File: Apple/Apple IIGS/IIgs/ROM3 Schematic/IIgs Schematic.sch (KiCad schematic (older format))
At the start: 0 parts

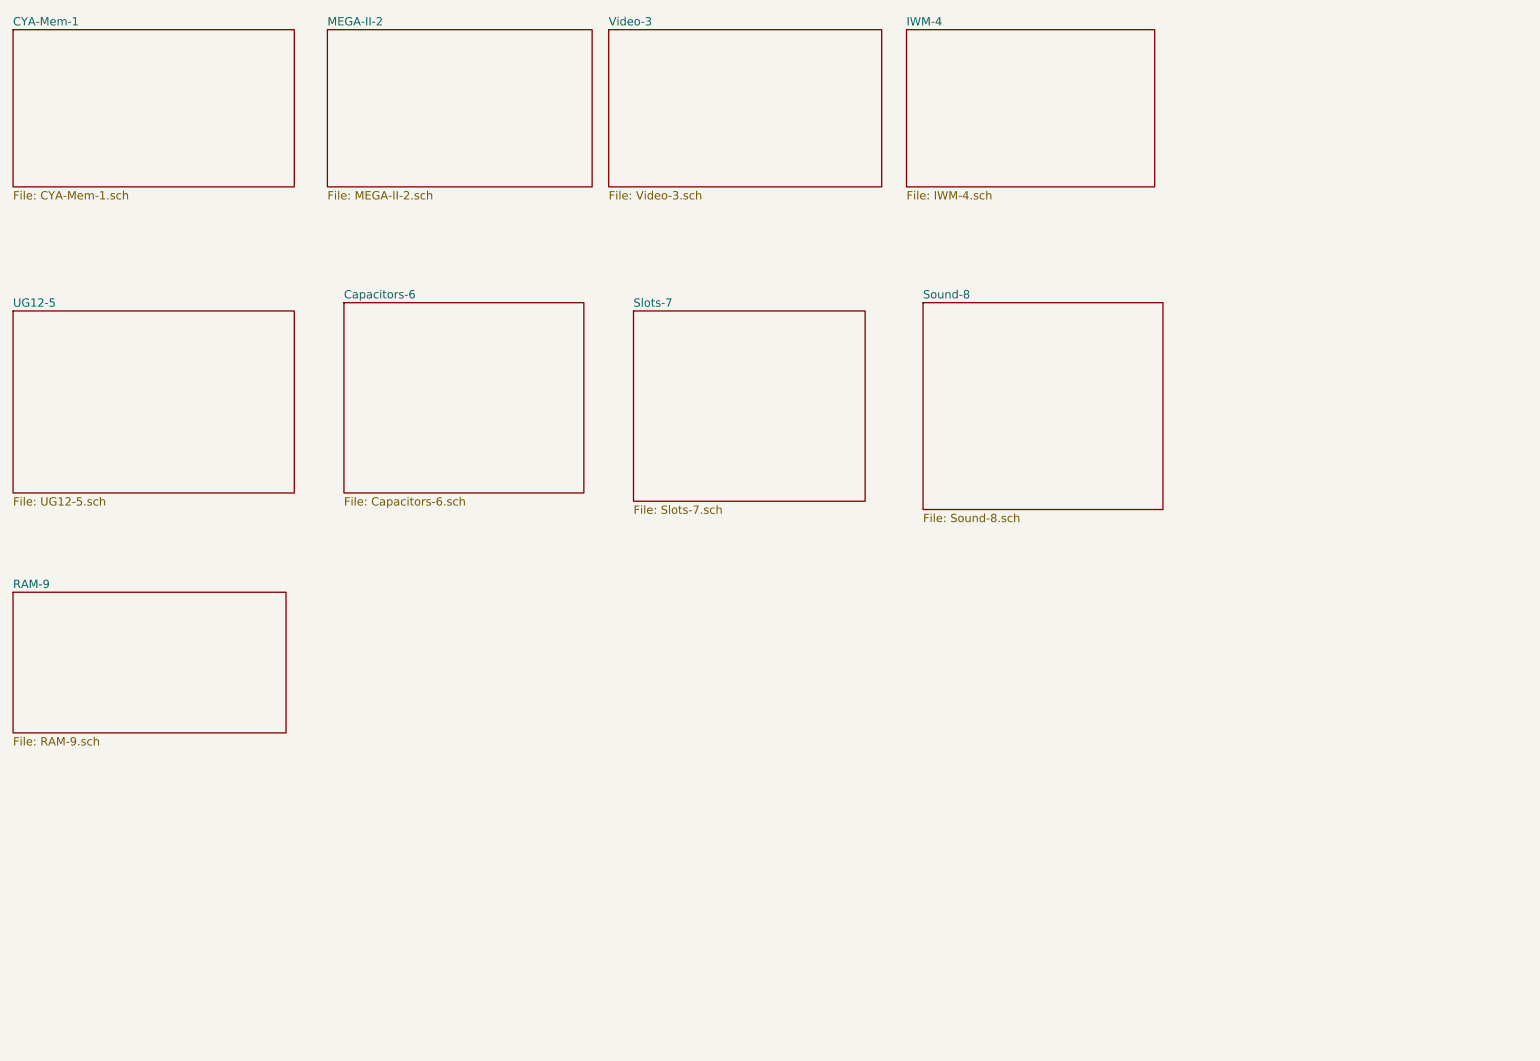
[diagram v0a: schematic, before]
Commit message: started v2 updates on iigs-rom3
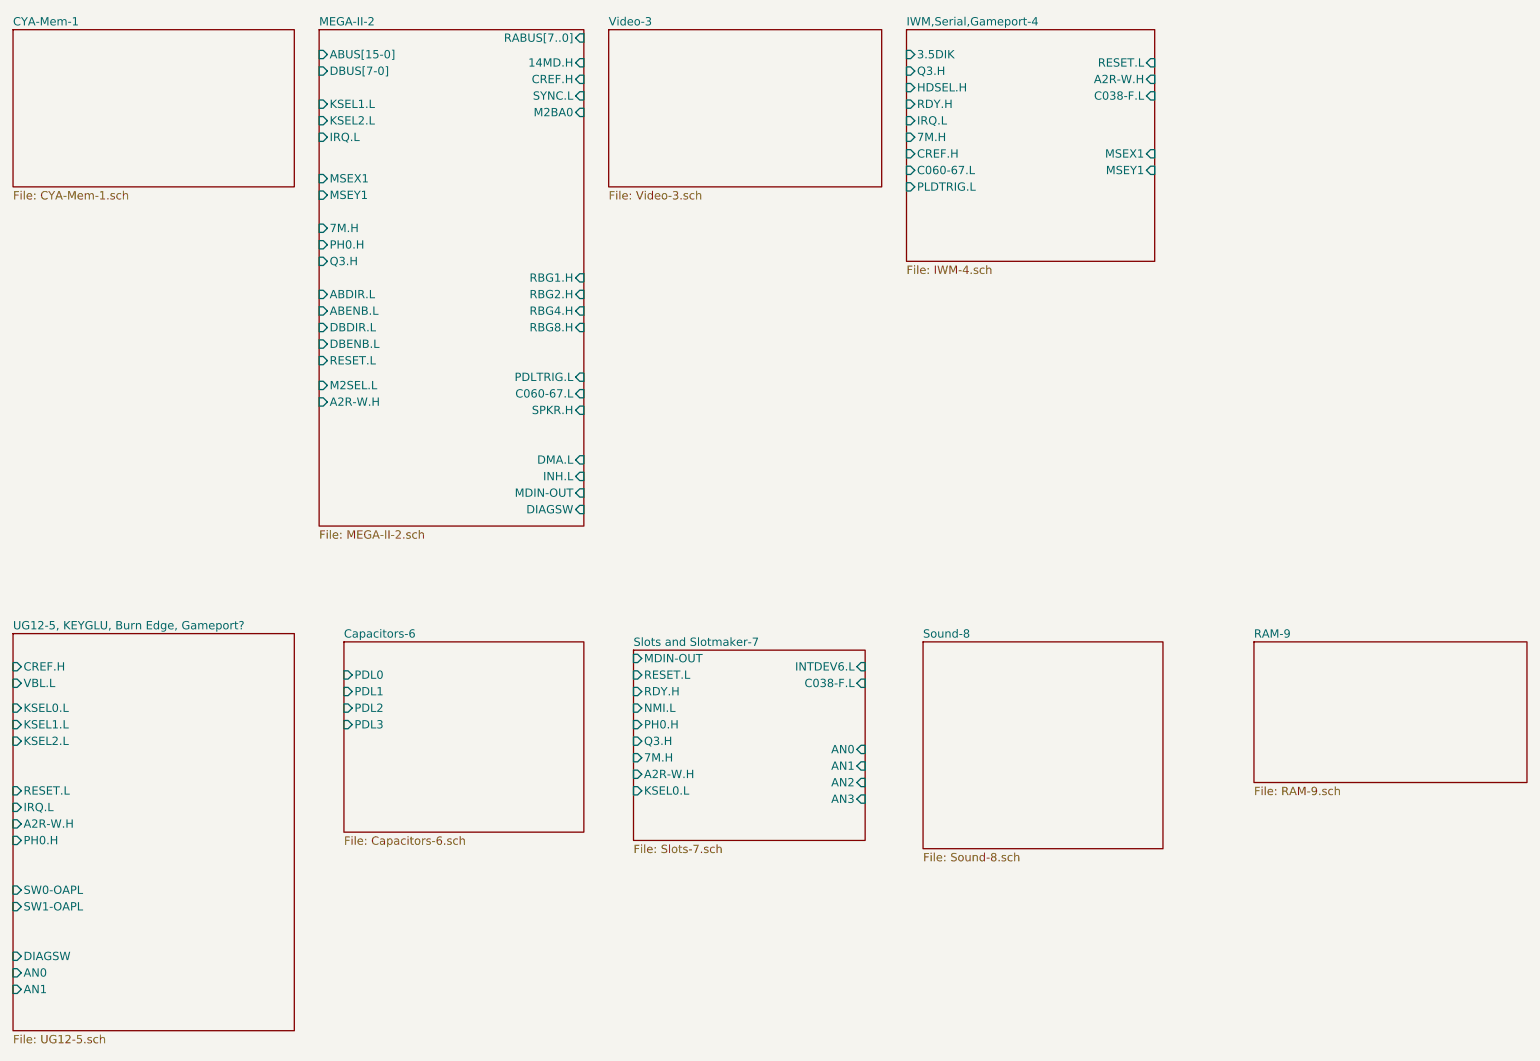
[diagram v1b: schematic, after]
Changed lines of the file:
@@
 Title ""
 Date ""
-Rev ""
+Rev "2"
 Comp ""
 Comment1 ""
@@
 $EndSheet
 $Sheet
-S 3100 1150 1600 950
-U 5BF1D236
-F0 "MEGA-II-2" 50
-F1 "MEGA-II-2.sch" 50
-$EndSheet
-$Sheet
 S 4800 1150 1650 950
 U 5BF1D7E4
@@
 $EndSheet
 $Sheet
-S 6600 1150 1500 950
+S 6600 1150 1500 1400
 U 5BF1EACB
-F0 "IWM-4" 50
+F0 "IWM,Serial,Gameport-4" 50
 F1 "IWM-4.sch" 50
+F2 "3.5DIK" I L 6600 1300 50
+F3 "Q3.H" I L 6600 1400 50
+F4 "HDSEL.H" I L 6600 1500 50
+F5 "RDY.H" I L 6600 1600 50
+F6 "IRQ.L" I L 6600 1700 50
+F7 "7M.H" I L 6600 1800 50
+F8 "CREF.H" I L 6600 1900 50
+F9 "MSEX1" I R 8100 1900 50
+F10 "MSEY1" I R 8100 2000 50
+F11 "RESET.L" I R 8100 1350 50
+F12 "A2R-W.H" I R 8100 1450 50
+F13 "C038-F.L" I R 8100 1550 50
+F14 "C060-67.L" I L 6600 2000 50
+F15 "PLDTRIG.L" I L 6600 2100 50
 $EndSheet
 $Sheet
-S 1200 2850 1700 1100
+S 1200 4800 1700 2400
 U 5BF204DB
-F0 "UG12-5" 50
+F0 "UG12-5, KEYGLU, Burn Edge, Gameport?" 50
 F1 "UG12-5.sch" 50
+F2 "CREF.H" I L 1200 5000 50
+F3 "KSEL0.L" I L 1200 5250 50
+F4 "KSEL1.L" I L 1200 5350 50
+F5 "KSEL2.L" I L 1200 5450 50
+F6 "RESET.L" I L 1200 5750 50
+F7 "VBL.L" I L 1200 5100 50
+F8 "DIAGSW" I L 1200 6750 50
+F9 "AN0" I L 1200 6850 50
+F10 "AN1" I L 1200 6950 50
+F11 "IRQ.L" I L 1200 5850 50
+F12 "A2R-W.H" I L 1200 5950 50
+F13 "PH0.H" I L 1200 6050 50
+F14 "SW0-OAPL" I L 1200 6350 50
+F15 "SW1-OAPL" I L 1200 6450 50
 $EndSheet
 $Sheet
-S 3200 2800 1450 1150
+S 3200 4850 1450 1150
 U 5BF20EB3
 F0 "Capacitors-6" 50
 F1 "Capacitors-6.sch" 50
+F2 "PDL3" I L 3200 5350 50
+F3 "PDL2" I L 3200 5250 50
+F4 "PDL1" I L 3200 5150 50
+F5 "PDL0" I L 3200 5050 50
 $EndSheet
 $Sheet
-S 4950 2850 1400 1150
+S 4950 4900 1400 1150
 U 5BF2158F
-F0 "Slots-7" 50
+F0 "Slots and Slotmaker-7" 50
 F1 "Slots-7.sch" 50
+F2 "RDY.H" I L 4950 5150 50
+F3 "NMI.L" I L 4950 5250 50
+F4 "PH0.H" I L 4950 5350 50
+F5 "Q3.H" I L 4950 5450 50
+F6 "7M.H" I L 4950 5550 50
+F7 "A2R-W.H" I L 4950 5650 50
+F8 "RESET.L" I L 4950 5050 50
+F9 "KSEL0.L" I L 4950 5750 50
+F10 "AN3" I R 6350 5800 50
+F11 "AN2" I R 6350 5700 50
+F12 "AN1" I R 6350 5600 50
+F13 "AN0" I R 6350 5500 50
+F14 "INTDEV6.L" I R 6350 5000 50
+F15 "C038-F.L" I R 6350 5100 50
+F16 "MDIN-OUT" I L 4950 4950 50
 $EndSheet
 $Sheet
-S 6700 2800 1450 1250
+S 6700 4850 1450 1250
 U 5BF22045
 F0 "Sound-8" 50
@@
 $EndSheet
 $Sheet
-S 1200 4550 1650 850
+S 8700 4850 1650 850
 U 5BF22CDE
 F0 "RAM-9" 50
 F1 "RAM-9.sch" 50
 $EndSheet
+$Sheet
+S 3050 1150 1600 3000
+U 5BF1D236
+F0 "MEGA-II-2" 50
+F1 "MEGA-II-2.sch" 50
+F2 "PDLTRIG.L" I R 4650 3250 50
+F3 "C060-67.L" I R 4650 3350 50
+F4 "SPKR.H" I R 4650 3450 50
+F5 "KSEL1.L" I L 3050 1600 50
+F6 "KSEL2.L" I L 3050 1700 50
+F7 "IRQ.L" I L 3050 1800 50
+F8 "MSEX1" I L 3050 2050 50
+F9 "MSEY1" I L 3050 2150 50
+F10 "DIAGSW" I R 4650 4050 50
+F11 "RESET.L" I L 3050 3150 50
+F12 "MDIN-OUT" I R 4650 3950 50
+F13 "DMA.L" I R 4650 3750 50
+F14 "M2SEL.L" I L 3050 3300 50
+F15 "M2BA0" I R 4650 1650 50
+F16 "INH.L" I R 4650 3850 50
+F17 "A2R-W.H" I L 3050 3400 50
+F18 "SYNC.L" I R 4650 1550 50
+F19 "14MD.H" I R 4650 1350 50
+F20 "7M.H" I L 3050 2350 50
+F21 "CREF.H" I R 4650 1450 50
+F22 "Q3.H" I L 3050 2550 50
+F23 "PH0.H" I L 3050 2450 50
+F24 "RBG8.H" I R 4650 2950 50
+F25 "RBG4.H" I R 4650 2850 50
+F26 "RBG2.H" I R 4650 2750 50
+F27 "RBG1.H" I R 4650 2650 50
+F28 "ABUS[15-0]" I L 3050 1300 50
+F29 "DBUS[7-0]" I L 3050 1400 50
+F30 "ABDIR.L" I L 3050 2750 50
+F31 "ABENB.L" I L 3050 2850 50
+F32 "DBDIR.L" I L 3050 2950 50
+F33 "DBENB.L" I L 3050 3050 50
+F34 "RABUS[7..0]" I R 4650 1200 50
+$EndSheet
 $EndSCHEMATC

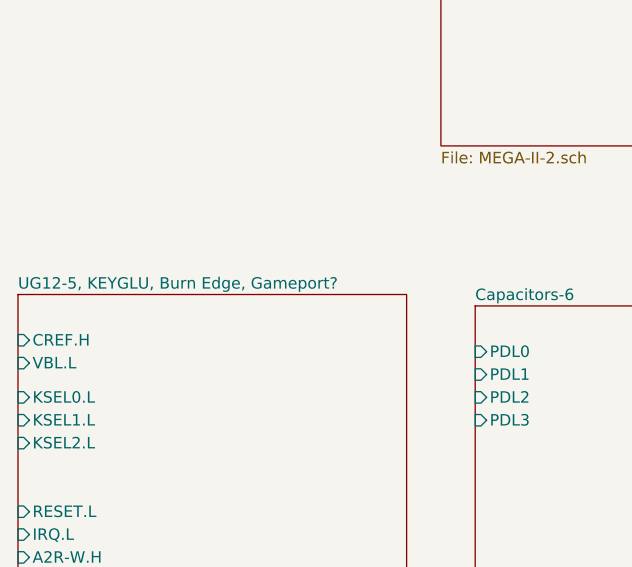
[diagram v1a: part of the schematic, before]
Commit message: added some notes, few rev2 changes, going to branch.
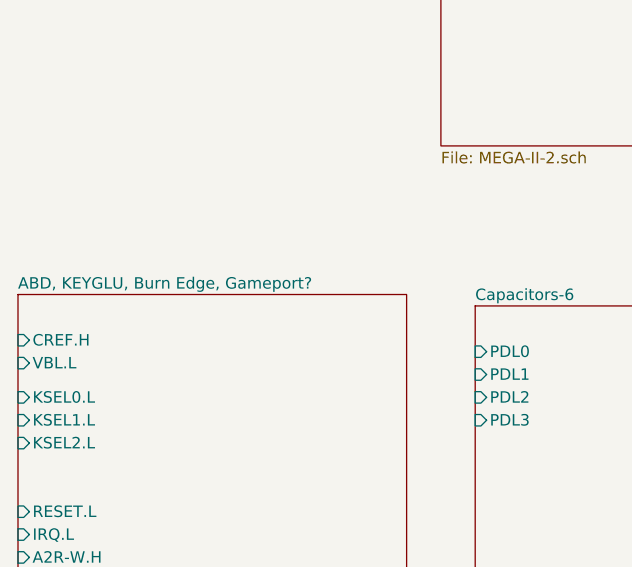
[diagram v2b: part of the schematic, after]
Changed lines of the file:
@@
 S 1200 4800 1700 2400
 U 5BF204DB
-F0 "UG12-5, KEYGLU, Burn Edge, Gameport?" 50
+F0 "ABD, KEYGLU, Burn Edge, Gameport?" 50
 F1 "UG12-5.sch" 50
 F2 "CREF.H" I L 1200 5000 50
